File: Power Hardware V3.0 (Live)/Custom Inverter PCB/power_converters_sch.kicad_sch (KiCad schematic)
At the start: 25 parts, among them J1 470531000, J11 470531000, J12 470531000, J13 470531000, J14 470531000, J15 470531000, J16 1714971, J8 1714971, U7 MIC5219-5.0YM5-TR

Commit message: Fixes
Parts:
- removed J1, J11, J12, J13, J14, J15: 470531000, CONN_SD-47053-001_H10p00_MOL, symbol 2025-06-22_18-08-57:470531000
- added J1, J11: 1990041, PHOENIX_1990041:PHOENIX_1990041, symbol PHOENIX_1990041:1990041
- added J17: 1714971, 1714971:PHOENIX_1714971, symbol 1714971:1714971
- C18, C19, C20, C22, C25, C26, C27, L1, R19, R20, R21, R22, U7, VR1: now not fitted
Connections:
- net +12V to relay: now also J17.2
- net Fan_Power: now also J1.1, J1.2, J1.3, J1.4, J1.5, J1.6
- net GND: now also J11.1, J11.2, J11.3, J11.4, J11.5, J11.6, J17.1
- no-connect marks 13 -> 1
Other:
- note added: "12V External Supply"
- note added: "IO"
- moved on the sheet: C16, C17, CR5

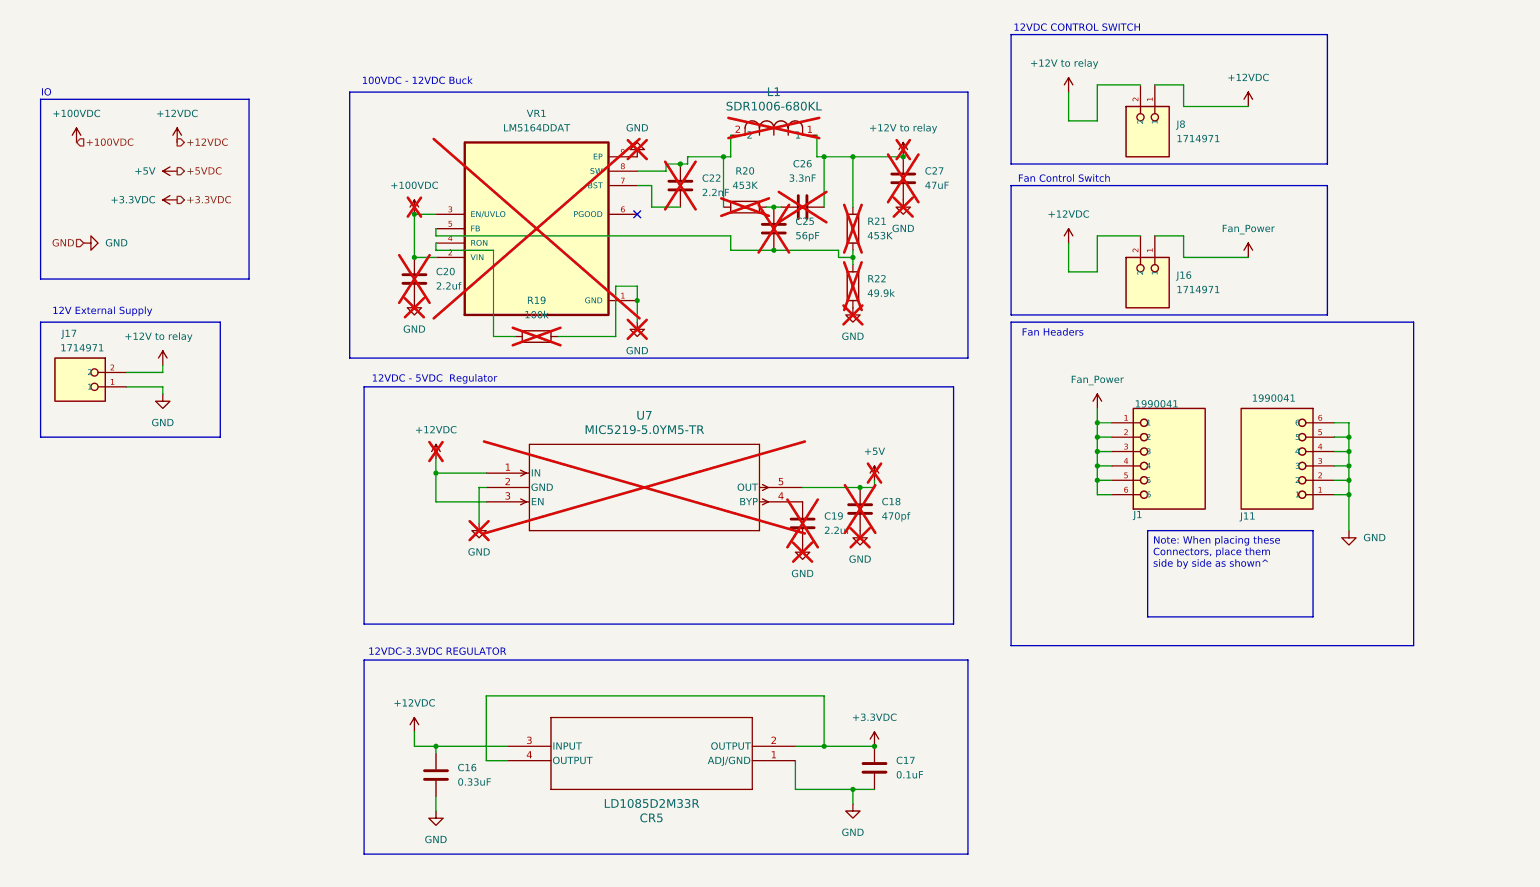
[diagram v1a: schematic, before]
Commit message: PCB V3 changes
-HV outputs and inputs changed to screw terminals for lugs
- Fuses changes to 50A
- ADC pin for temp sense along with the temp sensing circuit
- Added more pins to motor encoder term for temp sense
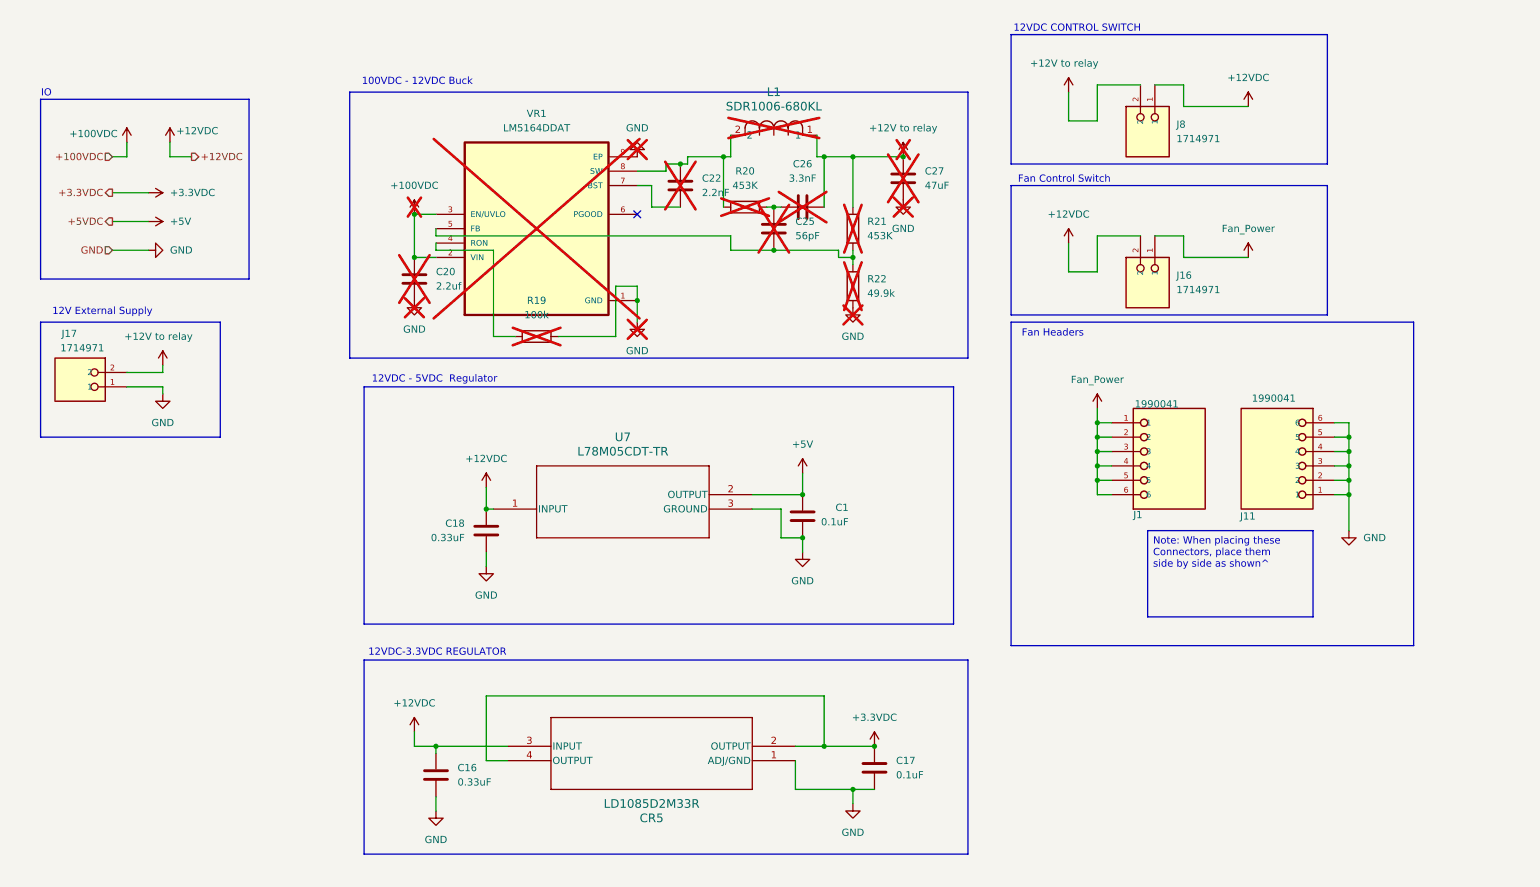
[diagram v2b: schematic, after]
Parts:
- removed C19: 2.2uf, Capacitor_SMD:C_0805_2012Metric, symbol Device:C
- removed U7: MIC5219-5.0YM5-TR, SOT-23-5_M5_MCH, symbol 2025-06-22_17-04-34:MIC5219-5.0YM5-TR
- added C1: 0.1uF, Capacitor_SMD:C_0805_2012Metric, symbol Device:C
- added U7: L78M05CDT-TR, L78M05CDT_TR:DPAK_STM-M, symbol 12-5V regulator L78M05CDT_TR:L78M05CDT-TR
- C18: value 470pf -> 0.33uF; Part Number C0805C471K5RACTU -> GRM219R71H334KA88D; now fitted
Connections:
- net +12VDC: now also C18.1, U7.1 (INPUT)
- net +5V: now also C1.1, U7.2 (OUTPUT); no longer C18.1
- net GND: now also C1.2, U7.3 (GROUND)

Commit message: PCB layout
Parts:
- removed J16, J17, J8: 1714971, 1714971:PHOENIX_1714971, symbol 1714971:1714971
- added J7: 1714971, 1714971:PHOENIX_1714971, symbol 1714971:1714971
- added J8, J9: 1990009, 2P term 1990009:PHOENIX_1990009, symbol 1990009 2P term:1990009
- renumbered C20 to C18, C16 to C19, C18 to C20, C22 to C21, C25 to C22, C26 to C23, C1 to C24, C17 to C25, C27 to C26, CR5 to CR4, J1 to J10, R19 to R29, R20 to R30, R21 to R31, R22 to R32
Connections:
- net +12V to relay: now also J7.2, J8.2
- net +12VDC: now also J8.1, J9.2
- net Fan_Power: now also J11.1, J11.3, J11.5, J9.1; no longer J10.2, J10.4, J10.6
- net GND: now also J10.2, J10.4, J10.6, J7.1; no longer J11.1, J11.3, J11.5
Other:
- moved on the sheet: J10, J11

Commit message: V3.0 is ordered
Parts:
- added D12: 12V, Capacitor_SMD:C_0603_1608Metric_Pad1.08x0.95mm_HandSolder, symbol Device:LED
- added D13: 5V, Capacitor_SMD:C_0603_1608Metric_Pad1.08x0.95mm_HandSolder, symbol Device:LED
- added D14: 3.3V, Capacitor_SMD:C_0603_1608Metric_Pad1.08x0.95mm_HandSolder, symbol Device:LED
- added R33, R34, R35, R36, R37: 220R, Resistor_SMD:R_0805_2012Metric, symbol Device:R
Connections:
- net +12V to relay: now also R33.2
- net +3.3VDC: now also R36.2, R37.2
- net +5V: now also R35.2
- net GND: now also D12.1 (K), D13.1 (K), D14.1 (K)
- new net: R33.1, R34.2
- new net: D14.2 (A), R36.1, R37.1
- new net: D13.2 (A), R35.1
- new net: D12.2 (A), R34.1
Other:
- note added: "12V INPUT ACTIVE LIGHT"
- note added: "3.3V ACTIVE LIGHT"
- note added: "5V ACTIVE LIGHT"

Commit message: V3 push
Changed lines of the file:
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@@
 	)
 	(rectangle
-		(start 76.2 78.74)
+		(start 73.66 78.74)
 		(end 180.34 120.65)
 		(stroke
@@
 	)
 	(rectangle
-		(start 76.2 127)
+		(start 73.66 127)
 		(end 182.88 161.29)
 		(stroke

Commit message: changes
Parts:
- C18, C21, C22, C23, C26, R29, R30, R31, R32: now left out of the parts list
- J7: Part Number (none) -> 1714971
- J8, J9: Part Number (none) -> 1990009
- L1: Part Number (none) -> SDR1006-680KL; now left out of the parts list
- U7: Part Number (none) -> L78M05CDT-TR
- VR1: Part Number (none) -> LM5164DDAT; now left out of the parts list
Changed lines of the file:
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@@
 		(unit 1)
 		(exclude_from_sim yes)
-		(in_bom yes)
+		(in_bom no)
 		(on_board no)
 		(dnp yes)
@@
 			)
 		)
+		(property "Part Number" "LM5164DDAT"
+			(at 106.68 50.8 0)
+			(effects
+				(font
+					(size 1.27 1.27)
+				)
+				(hide yes)
+			)
+		)
 		(pin "1"
 		)
@@
 		(unit 1)
 		(exclude_from_sim yes)
-		(in_bom yes)
+		(in_bom no)
 		(on_board no)
 		(dnp yes)
@@
 		(unit 1)
 		(exclude_from_sim yes)
-		(in_bom yes)
+		(in_bom no)
 		(on_board no)
 		(dnp yes)
@@
 		(unit 1)
 		(exclude_from_sim yes)
-		(in_bom yes)
+		(in_bom no)
 		(on_board no)
 		(dnp yes)
@@
 		(unit 1)
 		(exclude_from_sim yes)
-		(in_bom yes)
+		(in_bom no)
 		(on_board no)
 		(dnp yes)
@@
 		(unit 1)
 		(exclude_from_sim yes)
-		(in_bom yes)
+		(in_bom no)
 		(on_board no)
 		(dnp yes)
@@
 		(unit 1)
 		(exclude_from_sim yes)
-		(in_bom yes)
+		(in_bom no)
 		(on_board no)
 		(dnp yes)
@@
 		(unit 1)
 		(exclude_from_sim yes)
-		(in_bom yes)
+		(in_bom no)
 		(on_board no)
 		(dnp yes)
@@
 		(unit 1)
 		(exclude_from_sim yes)
-		(in_bom yes)
+		(in_bom no)
 		(on_board no)
 		(dnp yes)
@@
 		(unit 1)
 		(exclude_from_sim yes)
-		(in_bom yes)
+		(in_bom no)
 		(on_board no)
 		(dnp yes)
@@
 		(unit 1)
 		(exclude_from_sim yes)
-		(in_bom yes)
+		(in_bom no)
 		(on_board no)
 		(dnp yes)
@@
 		(unit 1)
 		(exclude_from_sim yes)
-		(in_bom yes)
+		(in_bom no)
 		(on_board no)
 		(dnp yes)
@@
 			)
 		)
+		(property "Part Number" "1990009"
+			(at 215.9 33.02 90)
+			(effects
+				(font
+					(size 1.27 1.27)
+				)
+				(hide yes)
+			)
+		)
 		(pin "1"
 		)
@@
 			)
 		)
+		(property "Part Number" "L78M05CDT-TR"
+			(at 99.06 100.33 0)
+			(effects
+				(font
+					(size 1.27 1.27)
+				)
+				(hide yes)
+			)
+		)
 		(pin "1"
 		)
@@
 		(unit 1)
 		(exclude_from_sim yes)
-		(in_bom yes)
+		(in_bom no)
 		(on_board no)
 		(dnp yes)
@@
 			)
 		)
+		(property "Part Number" "SDR1006-680KL"
+			(at 140.97 34.29 0)
+			(effects
+				(font
+					(size 1.27 1.27)
+				)
+				(hide yes)
+			)
+		)
 		(pin "2"
 		)
@@
 		(unit 1)
 		(exclude_from_sim yes)
-		(in_bom yes)
+		(in_bom no)
 		(on_board no)
 		(dnp yes)
@@
 		(unit 1)
 		(exclude_from_sim yes)
-		(in_bom yes)
+		(in_bom no)
 		(on_board no)
 		(dnp yes)
@@
 		(unit 1)
 		(exclude_from_sim yes)
-		(in_bom yes)
+		(in_bom no)
 		(on_board no)
 		(dnp yes)
@@
 			)
 		)
+		(property "Part Number" "1714971"
+			(at 26.67 78.74 0)
+			(effects
+				(font
+					(size 1.27 1.27)
+				)
+				(hide yes)
+			)
+		)
 		(pin "2"
 		)
@@
 			)
 		)
+		(property "Part Number" "1990009"
+			(at 215.9 59.69 90)
+			(effects
+				(font
+					(size 1.27 1.27)
+				)
+				(hide yes)
+			)
+		)
 		(pin "1"
 		)
@@
 		(unit 1)
 		(exclude_from_sim yes)
-		(in_bom yes)
+		(in_bom no)
 		(on_board no)
 		(dnp yes)
@@
 		(unit 1)
 		(exclude_from_sim yes)
-		(in_bom yes)
+		(in_bom no)
 		(on_board no)
 		(dnp yes)
